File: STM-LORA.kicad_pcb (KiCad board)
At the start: 2 copper layers, 56.5 x 53.3 mm, 52 parts, among them J1 Batt, J10 CONN_02X07, J11 CONN_02X09, J12 CONN_01X02, J13 CONN_01X02, J14 CONN_01X02, J15 CONN_01X03, J16 CONN_01X01, J2 Solar, J3 CONN_01X17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

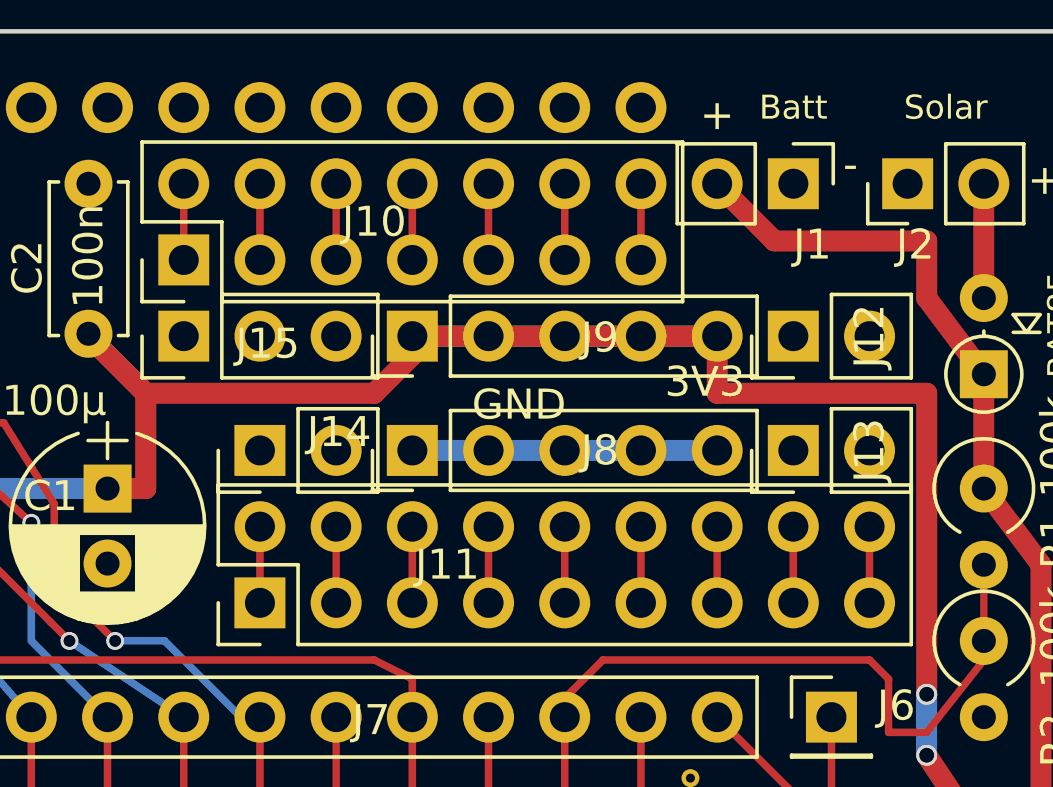
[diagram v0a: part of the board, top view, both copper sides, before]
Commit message: restore breadboard tracks on bot sides
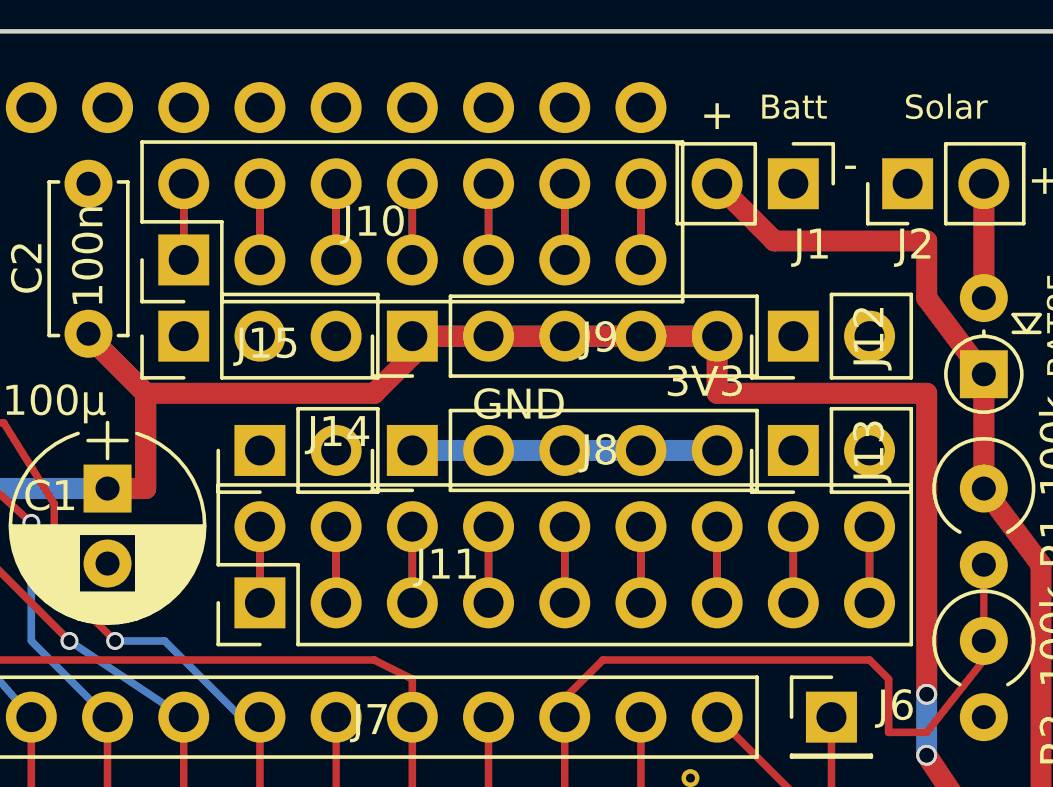
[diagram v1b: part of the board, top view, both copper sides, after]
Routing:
- net Net-(J11-Pad7): track 2.54 -> 5.08 mm
- net Net-(J11-Pad5): track 2.54 -> 5.08 mm
- net Net-(J11-Pad3): track 2.54 -> 5.08 mm
- net Net-(J11-Pad17): track 2.54 -> 5.08 mm
- net Net-(J11-Pad15): track 2.54 -> 5.08 mm
- net Net-(J11-Pad13): track 2.54 -> 5.08 mm
- net Net-(J11-Pad11): track 2.54 -> 5.08 mm
- net Net-(J11-Pad10): track 2.54 -> 5.08 mm
- net Net-(J11-Pad1): track 2.54 -> 5.08 mm
- net Net-(J10-Pad7): track 2.54 -> 5.08 mm
- net Net-(J10-Pad5): track 2.54 -> 5.08 mm
- net Net-(J10-Pad3): track 2.54 -> 5.08 mm
- net Net-(J10-Pad13): track 2.54 -> 5.08 mm
- net Net-(J10-Pad11): track 2.54 -> 5.08 mm
- net Net-(J10-Pad10): track 2.54 -> 5.08 mm
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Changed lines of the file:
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@@
     (links 108)
     (no_connects 0)
-    (area 81.834667 52.448 140.648 109.173333)
+    (area 83.744999 53.264999 140.410001 106.755001)
     (thickness 1.6)
     (drawings 12)
-    (tracks 178)
+    (tracks 195)
     (zones 0)
     (modules 52)
@@
       (effects (font (size 1 1) (thickness 0.15)))
     )
-    (fp_text value CONN_01X01 (at 0 2.33) (layer F.Fab)
+    (fp_text value CONN_01X01 (at 0 2.33) (layer F.Fab) hide
       (effects (font (size 1 1) (thickness 0.15)))
     )
@@
   (segment (start 137.16 58.42) (end 137.16 62.23) (width 0.7) (layer F.Cu) (net 42) (status 30))
   (segment (start 110.49 58.42) (end 110.49 60.96) (width 0.25) (layer F.Cu) (net 43))
+  (segment (start 110.49 58.42) (end 110.49 59.622081) (width 0.25) (layer B.Cu) (net 43))
+  (segment (start 110.49 59.622081) (end 110.49 60.96) (width 0.25) (layer B.Cu) (net 43))
   (segment (start 113.03 58.42) (end 113.03 60.96) (width 0.25) (layer F.Cu) (net 44))
+  (segment (start 113.03 58.42) (end 113.03 60.96) (width 0.25) (layer B.Cu) (net 44))
   (segment (start 115.57 58.42) (end 115.57 60.96) (width 0.25) (layer F.Cu) (net 45))
+  (segment (start 115.57 58.42) (end 115.57 60.96) (width 0.25) (layer B.Cu) (net 45))
   (segment (start 118.11 58.42) (end 118.11 60.96) (width 0.25) (layer F.Cu) (net 46))
+  (segment (start 118.11 58.42) (end 118.11 60.96) (width 0.25) (layer B.Cu) (net 46))
   (segment (start 120.65 58.42) (end 120.65 60.96) (width 0.25) (layer F.Cu) (net 47))
+  (segment (start 120.65 58.42) (end 120.65 60.96) (width 0.25) (layer B.Cu) (net 47))
   (segment (start 123.19 58.42) (end 123.19 60.96) (width 0.25) (layer F.Cu) (net 48))
+  (segment (start 123.19 58.42) (end 123.19 60.96) (width 0.25) (layer B.Cu) (net 48))
   (segment (start 125.73 58.42) (end 125.73 60.96) (width 0.25) (layer F.Cu) (net 49))
-  (segment (start 113.03 72.39) (end 113.03 69.85) (width 0.25) (layer F.Cu) (net 50))
+  (segment (start 125.73 58.42) (end 125.73 60.96) (width 0.25) (layer B.Cu) (net 49))
+  (segment (start 113.03 69.85) (end 113.03 72.39) (width 0.25) (layer F.Cu) (net 50))
+  (segment (start 113.03 69.85) (end 113.03 72.39) (width 0.25) (layer B.Cu) (net 50))
   (segment (start 115.57 69.85) (end 115.57 72.39) (width 0.25) (layer F.Cu) (net 51))
-  (segment (start 118.11 72.39) (end 118.11 69.85) (width 0.25) (layer F.Cu) (net 52))
+  (segment (start 115.57 69.85) (end 115.57 72.39) (width 0.25) (layer B.Cu) (net 51))
+  (segment (start 118.11 69.85) (end 118.11 72.39) (width 0.25) (layer F.Cu) (net 52))
+  (segment (start 118.11 69.85) (end 118.11 72.39) (width 0.25) (layer B.Cu) (net 52))
   (segment (start 120.65 69.85) (end 120.65 72.39) (width 0.25) (layer F.Cu) (net 53))
-  (segment (start 123.19 72.39) (end 123.19 69.85) (width 0.25) (layer F.Cu) (net 54))
+  (segment (start 120.65 69.85) (end 120.65 72.39) (width 0.25) (layer B.Cu) (net 53))
+  (segment (start 123.19 69.85) (end 123.19 72.39) (width 0.25) (layer F.Cu) (net 54))
+  (segment (start 123.19 69.85) (end 123.19 72.39) (width 0.25) (layer B.Cu) (net 54))
   (segment (start 125.73 69.85) (end 125.73 72.39) (width 0.25) (layer F.Cu) (net 55))
-  (segment (start 128.27 72.39) (end 128.27 69.85) (width 0.25) (layer F.Cu) (net 56))
+  (segment (start 125.73 69.85) (end 125.73 72.39) (width 0.25) (layer B.Cu) (net 55))
+  (segment (start 128.27 69.85) (end 128.27 72.39) (width 0.25) (layer F.Cu) (net 56))
+  (segment (start 128.27 69.85) (end 128.27 72.39) (width 0.25) (layer B.Cu) (net 56))
   (segment (start 130.81 69.85) (end 130.81 72.39) (width 0.25) (layer F.Cu) (net 57))
-  (segment (start 133.35 72.39) (end 133.35 69.85) (width 0.25) (layer F.Cu) (net 58))
+  (segment (start 130.81 69.85) (end 130.81 72.39) (width 0.25) (layer B.Cu) (net 57))
+  (segment (start 133.35 69.85) (end 133.35 72.39) (width 0.25) (layer F.Cu) (net 58))
+  (segment (start 133.35 69.85) (end 133.35 72.39) (width 0.25) (layer B.Cu) (net 58))
   (segment (start 86.87 58.39) (end 86.87 55.755) (width 0.5) (layer F.Cu) (net 68))
   (segment (start 86.87 55.755) (end 86.868 55.753) (width 0.25) (layer F.Cu) (net 68))

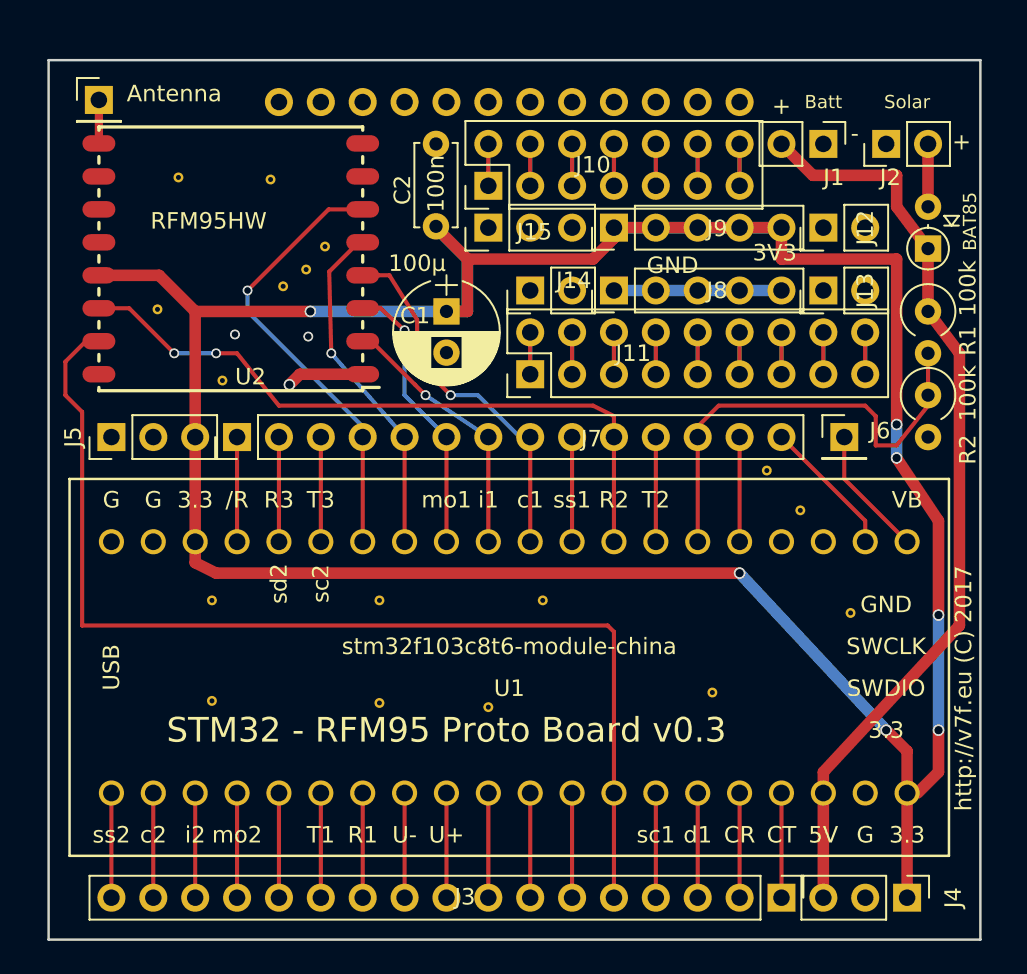
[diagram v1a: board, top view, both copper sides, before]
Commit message: Change GND plane and add 3v3 track
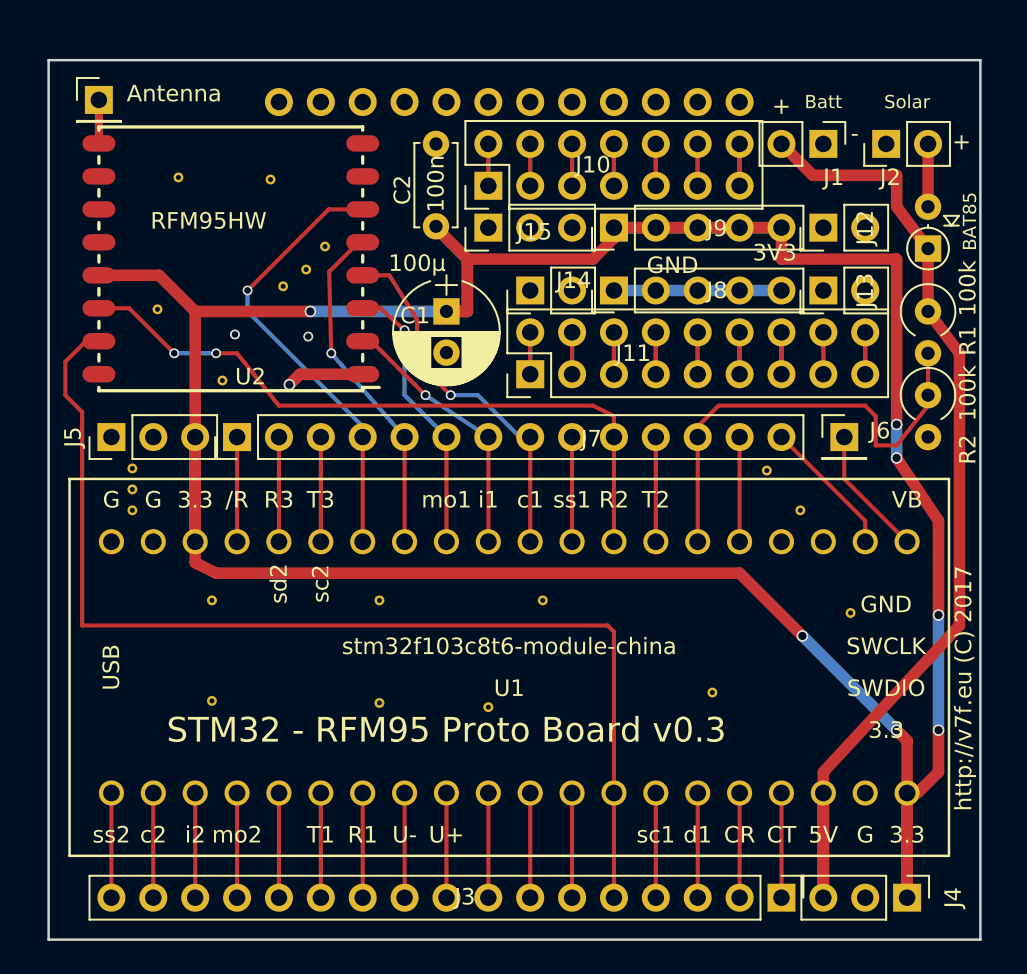
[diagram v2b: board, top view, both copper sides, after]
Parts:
- added REF**: VIA-0.6mm, VIA-0.6mm, F.Cu at (88.9, 78.1)
- added REF**: VIA-0.6mm, VIA-0.6mm, F.Cu at (88.9, 79.4)
- added REF**: VIA-0.6mm, VIA-0.6mm, F.Cu at (88.9, 80.6)
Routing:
- net /3V3: track 182.1 -> 195.0 mm
- net VCC: track 56.1 -> 62.5 mm
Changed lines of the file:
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@@
 (kicad_pcb (version 4) (host pcbnew 4.0.6-e0-6349~53~ubuntu16.04.1)
   (general
-    (links 108)
+    (links 111)
     (no_connects 0)
-    (area 83.744999 53.264999 140.410001 106.755001)
+    (area 81.834667 52.448 140.648 109.173333)
     (thickness 1.6)
     (drawings 12)
-    (tracks 195)
+    (tracks 199)
     (zones 0)
-    (modules 52)
+    (modules 55)
     (nets 69)
   )
@@
     (add_net GND)
     (add_net VCC)
+  )
+  (module VIA-0.6mm (layer F.Cu)
+    (at 88.9 78.105)
+    (fp_text reference REF** (at 0 0.5) (layer F.SilkS) hide
+      (effects (font (size 0.127 0.127) (thickness 0.015)))
+    )
+    (fp_text value VIA-0.6mm (at 0 -0.5) (layer F.Fab) hide
+      (effects (font (size 0.127 0.127) (thickness 0.015)))
+    )
+    (pad 1 thru_hole circle (at 0 0) (size 0.6 0.6) (drill 0.3) (layers *.Cu)
+      (net 7 GND) (zone_connect 2))
+  )
+  (module VIA-0.6mm (layer F.Cu)
+    (at 88.9 79.375)
+    (fp_text reference REF** (at 0 0.5) (layer F.SilkS) hide
+      (effects (font (size 0.127 0.127) (thickness 0.015)))
+    )
+    (fp_text value VIA-0.6mm (at 0 -0.5) (layer F.Fab) hide
+      (effects (font (size 0.127 0.127) (thickness 0.015)))
+    )
+    (pad 1 thru_hole circle (at 0 0) (size 0.6 0.6) (drill 0.3) (layers *.Cu)
+      (net 7 GND) (zone_connect 2))
+  )
+  (module VIA-0.6mm (layer F.Cu)
+    (at 88.9 80.645)
+    (fp_text reference REF** (at 0 0.5) (layer F.SilkS) hide
+      (effects (font (size 0.127 0.127) (thickness 0.015)))
+    )
+    (fp_text value VIA-0.6mm (at 0 -0.5) (layer F.Fab) hide
+      (effects (font (size 0.127 0.127) (thickness 0.015)))
+    )
+    (pad 1 thru_hole circle (at 0 0) (size 0.6 0.6) (drill 0.3) (layers *.Cu)
+      (net 7 GND) (zone_connect 2))
   )
   (module Exp-Area-Pad (layer F.Cu)
@@
   (segment (start 102.87 72.39) (end 99.06 72.39) (width 0.7) (layer F.Cu) (net 7) (status 10))
   (segment (start 99.06 72.39) (end 98.425 73.025) (width 0.7) (layer F.Cu) (net 7))
+  (segment (start 130.81 104.14) (end 130.81 97.79) (width 0.7) (layer B.Cu) (net 8))
   (segment (start 130.81 97.79) (end 130.81 104.14) (width 0.7) (layer F.Cu) (net 8) (status 30))
   (segment (start 135.255 60.325) (end 135.255 62.23) (width 0.7) (layer F.Cu) (net 8))
@@
   (segment (start 90.17 97.79) (end 90.17 104.14) (width 0.25) (layer F.Cu) (net 24) (status 30))
   (segment (start 87.63 104.14) (end 87.63 97.79) (width 0.25) (layer F.Cu) (net 25) (status 30))
+  (segment (start 135.604999 94.329999) (end 135.255 93.98) (width 0.7) (layer F.Cu) (net 26))
+  (segment (start 135.89 94.615) (end 135.604999 94.329999) (width 0.7) (layer F.Cu) (net 26))
+  (segment (start 135.89 97.79) (end 135.89 94.615) (width 0.7) (layer F.Cu) (net 26))
+  (segment (start 129.54 88.265) (end 135.255 93.98) (width 0.7) (layer B.Cu) (net 26))
+  (via (at 135.255 93.98) (size 0.7) (drill 0.5) (layers F.Cu B.Cu) (net 26))
+  (segment (start 125.73 84.455) (end 129.54 88.265) (width 0.7) (layer F.Cu) (net 26))
+  (via (at 129.54 88.265) (size 0.7) (drill 0.5) (layers F.Cu B.Cu) (net 26))
+  (segment (start 125.73 84.455) (end 93.98 84.455) (width 0.7) (layer F.Cu) (net 26))
+  (segment (start 92.71 82.55) (end 92.71 76.2) (width 0.7) (layer B.Cu) (net 26))
+  (segment (start 135.89 104.14) (end 135.89 97.79) (width 0.7) (layer B.Cu) (net 26))
   (segment (start 109.22 68.58) (end 107.95 68.58) (width 0.7) (layer F.Cu) (net 26))
   (segment (start 128.27 63.5) (end 128.27 65.405) (width 0.7) (layer F.Cu) (net 26) (status 10))
@@
   (segment (start 123.19 63.5) (end 125.73 63.5) (width 0.7) (layer F.Cu) (net 26) (status 30))
   (segment (start 125.73 63.5) (end 128.27 63.5) (width 0.7) (layer F.Cu) (net 26) (status 30))
-  (segment (start 135.89 97.79) (end 135.89 95.25) (width 0.7) (layer F.Cu) (net 26) (status 10))
   (segment (start 92.71 83.82) (end 92.71 82.55) (width 0.7) (layer F.Cu) (net 26) (status 20))
   (segment (start 93.98 84.455) (end 92.71 83.82) (width 0.7) (layer F.Cu) (net 26))
-  (segment (start 125.73 84.455) (end 93.98 84.455) (width 0.7) (layer F.Cu) (net 26))
-  (segment (start 125.73 84.455) (end 125.73 84.455) (width 0.7) (layer F.Cu) (net 26))
-  (via (at 125.73 84.455) (size 0.7) (drill 0.5) (layers F.Cu B.Cu) (net 26))
-  (segment (start 134.62 93.98) (end 125.73 84.455) (width 0.7) (layer B.Cu) (net 26))
-  (via (at 134.62 93.98) (size 0.7) (drill 0.5) (layers F.Cu B.Cu) (net 26))
-  (segment (start 135.89 95.25) (end 134.62 93.98) (width 0.7) (layer F.Cu) (net 26))
   (segment (start 109.22 68.58) (end 99.695 68.58) (width 0.7) (layer B.Cu) (net 26) (status 10))
   (segment (start 99.695 68.58) (end 92.71 68.58) (width 0.7) (layer F.Cu) (net 26))
